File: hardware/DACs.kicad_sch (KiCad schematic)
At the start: 44 parts, among them J10 Conn_Coaxial, J11 Conn_Coaxial, J12 Conn_Coaxial, J9 Conn_Coaxial, U10 LTC2642, U21 LTC2642, U26 REF35250QDBVR, U4 OPA2994xD, U5 OPA2994xD, U6 LTC2642, U7 OPA2994xD, U8 OPA2994xD, U9 LTC2642

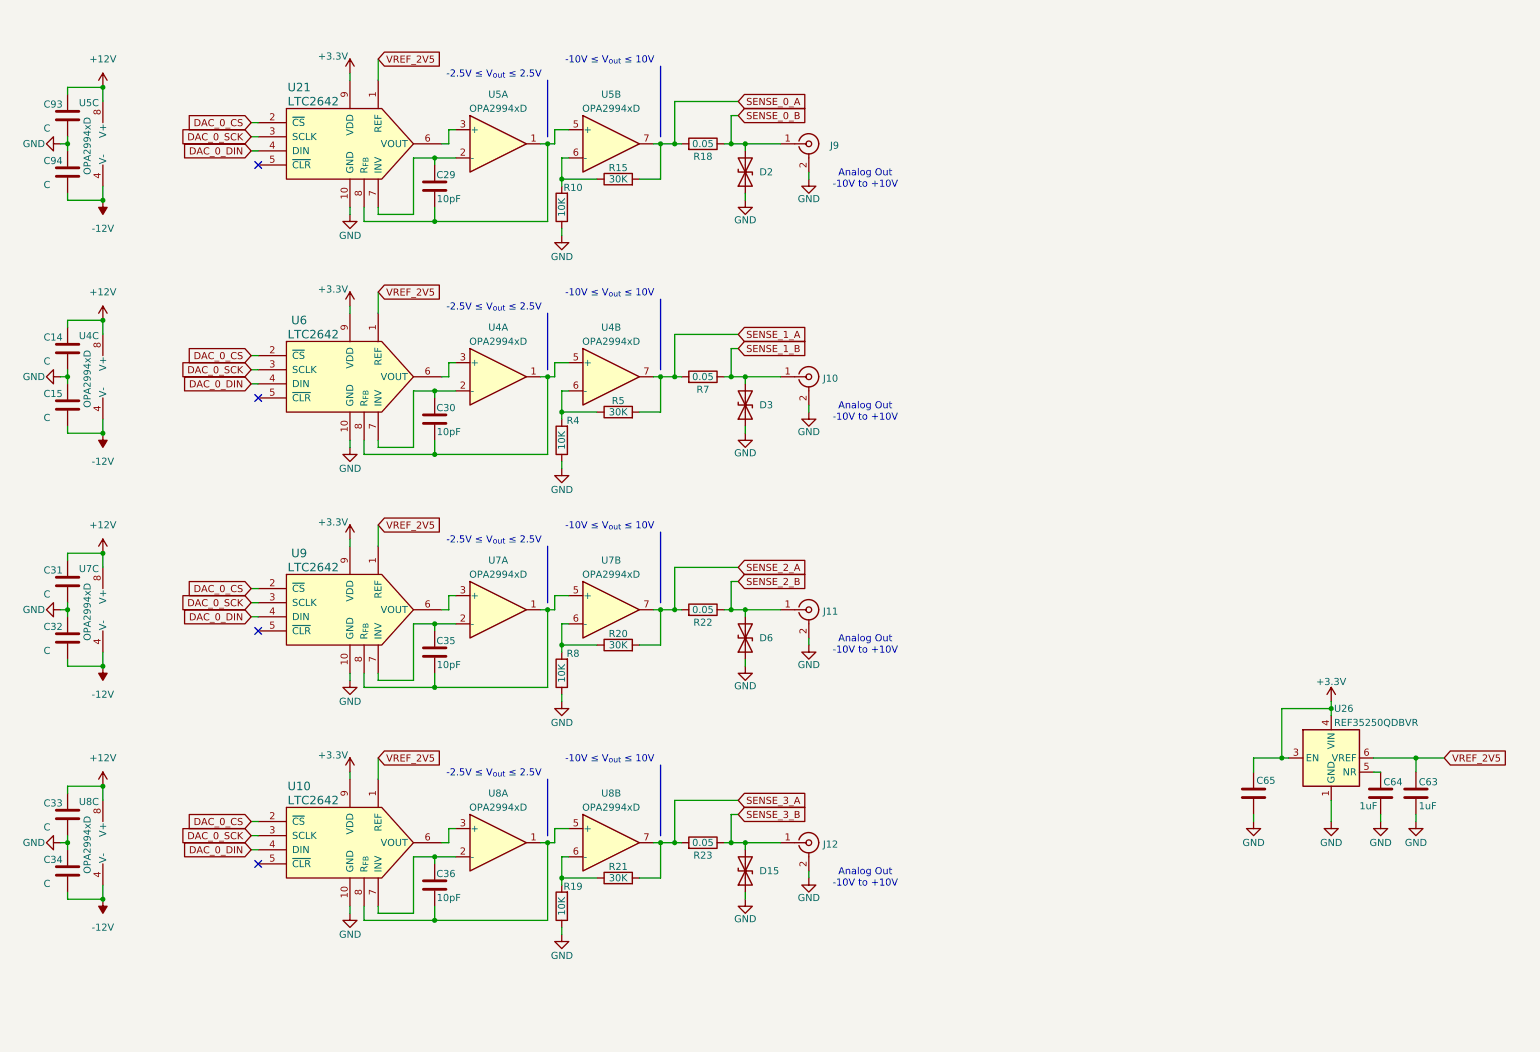
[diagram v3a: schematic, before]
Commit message: update short detection; draft bom
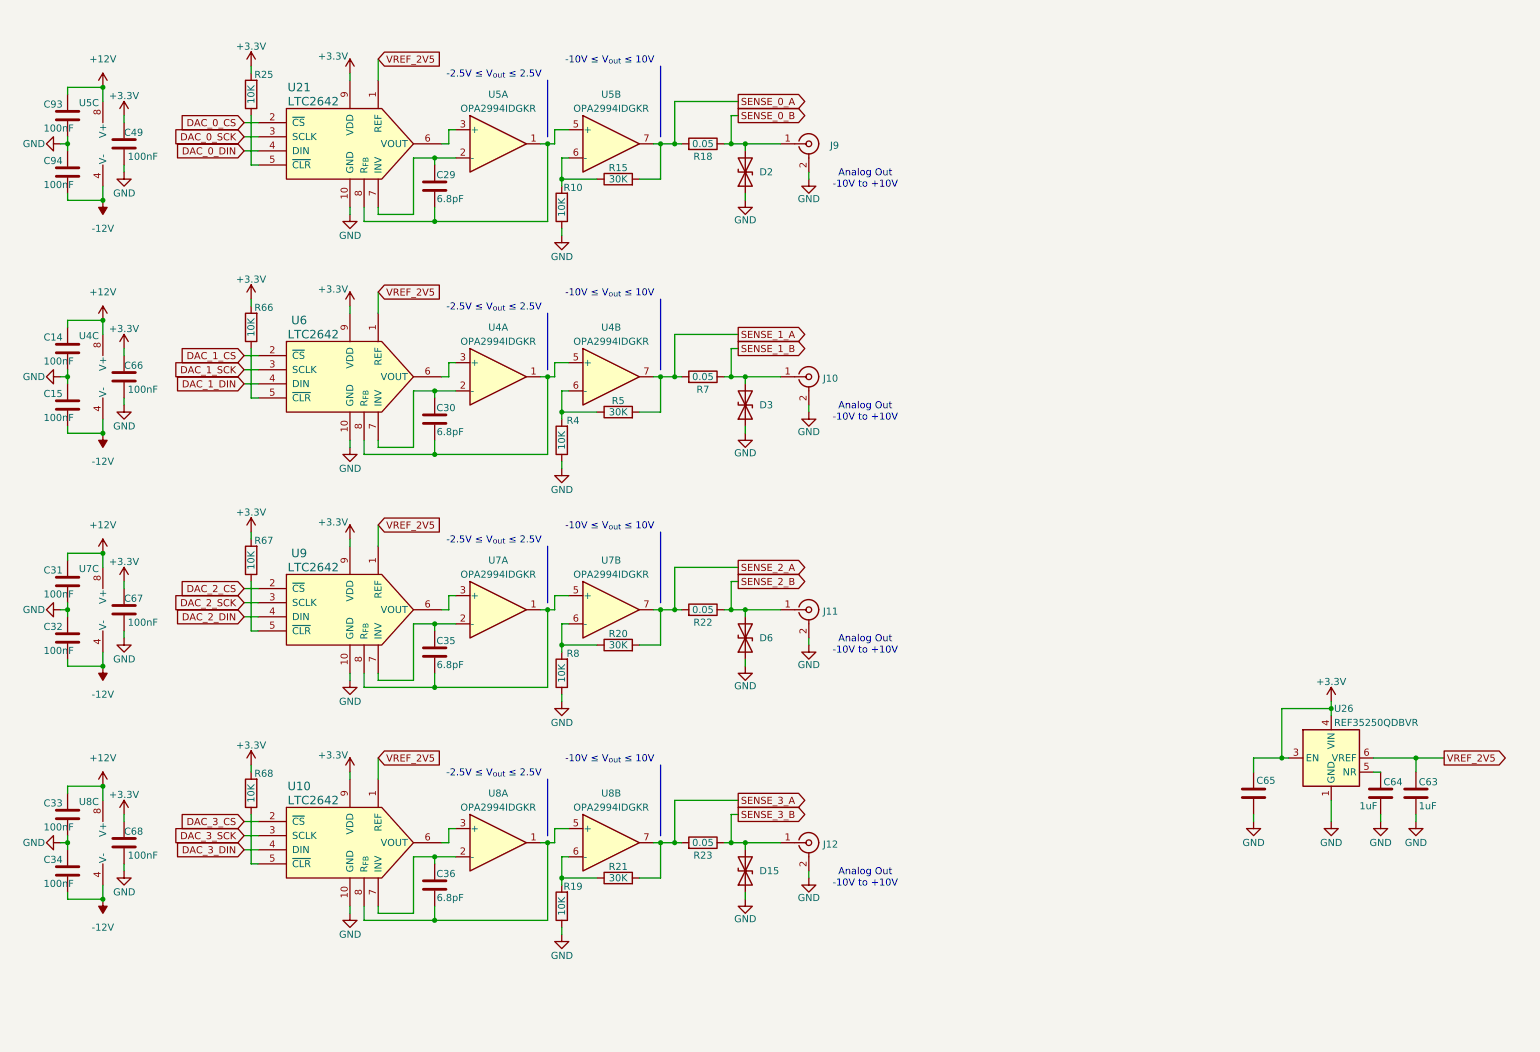
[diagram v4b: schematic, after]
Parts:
- added C49, C66, C67, C68: 100nF, Capacitor_SMD:C_0402_1005Metric, symbol harp.device.quad.dac:C_0603
- added R25, R66, R67, R68: 10K, Resistor_SMD:R_0402_1005Metric, symbol Device:R
- C14, C15, C31, C32, C33, C34, C93, C94: value C -> 100nF; footprint (none) -> Capacitor_SMD:C_0402_1005Metric; Link (none) -> https://www.digikey.com/en/products/detail/murata-electroni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; Manufacturer (none) -> Murata Electronics; Manufacturer Number (none) -> GRM155R71H104KE14D; Temperature Coefficient (none) -> X7R
- C29, C30, C35, C36: value 10pF -> 6.8pF; footprint (none) -> Capacitor_SMD:C_0402_1005Metric; Link (none) -> https://www.digikey.com/en/products/detail/murata-electroni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; Manufacturer (none) -> Murata Electronics; Manufacturer Number (none) -> GCM1555C1H6R8BA16J; Temperature Coefficient (none) -> C0G/NP0
- C63, C64: Manufacturer_Name TDK -> (none); Manufacturer_Part_Number C1608X7R1H105K080AB -> (none)
- C65: footprint Capacitor_SMD:C_0603_1608Metric -> Capacitor_SMD:C_0402_1005Metric; Link https://www.digikey.com/en/products/detail/kemet/C0603C104K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 -> https://www.digikey.com/en/products/detail/murata-electroni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; Manufacturer KEMET -> Murata Electronics; Manufacturer Number C0603C104K5RACTU -> GRM155R71H104KE14D; Manufacturer_Name KEMET -> (none); Manufacturer_Part_Number C0603C104K5RACTU -> (none); PCBWay Link https://www.pcbway.com/components/detail/0402B104K160CT/307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 -> (none); Temperature Coefficient (none) -> X7R
- R10, R15, R19, R20, R21, R4, R5, R8: footprint (none) -> Resistor_SMD:R_0402_1005Metric
- R18, R22, R23, R7: footprint (none) -> Resistor_SMD:R_0402_1005Metric; Link (none) -> https://www.digikey.com/en/products/detail/panasonic-electr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; Manufacturer (none) -> Panasonic Electronic Components; Manufacturer Number (none) -> ERJ-2BWFR050X
- U10, U21, U6, U9: footprint (none) -> Package_SO:MSOP-10_3x3mm_P0.5mm
- U4, U5, U7, U8: value OPA2994xD -> OPA2994IDGKR; footprint Package_SO:SOIC-8_3.9x4.9mm_P1.27mm -> Package_SO:VSSOP-8_3x3mm_P0.65mm; Manufacturer (none) -> Texas Instruments; Manufacturer Number (none) -> OPA2994IDGKR
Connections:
- net +3.3V: now also C49.2, C66.2, C67.2, C68.2, R25.2, R66.2, R67.2, R68.2
- net DAC_0_CS: no longer U10.2 (~{CS}), U6.2 (~{CS}), U9.2 (~{CS})
- net DAC_0_DIN: no longer U10.4 (DIN), U6.4 (DIN), U9.4 (DIN)
- net DAC_0_SCK: no longer U10.3 (SCLK), U6.3 (SCLK), U9.3 (SCLK)
- net GND: now also C49.1, C66.1, C67.1, C68.1
- net at U10.5 (~{CLR}): now also R68.1
- net at U9.5 (~{CLR}): now also R67.1
- net at U6.5 (~{CLR}): now also R66.1
- net at U21.5 (~{CLR}): now also R25.1
- new net DAC_1_CS: U6.2 (~{CS})
- new net DAC_1_DIN: U6.4 (DIN)
- new net DAC_1_SCK: U6.3 (SCLK)
- new net DAC_2_CS: U9.2 (~{CS})
- new net DAC_2_DIN: U9.4 (DIN)
- new net DAC_2_SCK: U9.3 (SCLK)
- new net DAC_3_CS: U10.2 (~{CS})
- new net DAC_3_DIN: U10.4 (DIN)
- new net DAC_3_SCK: U10.3 (SCLK)
- no-connect marks 4 -> 0

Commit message: update board draft
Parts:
- J6: renamed from J9; footprint harp.device.quad.dac.kicad:SMA_TE_Connectivity_CONSMA002-SMD-G-T_Horizontal -> kicad-lib:BNC_TEConnectivity_CONBNC001_Vertical; Link https://www.digikey.com/en/products/detail/te-connectivity-linx/CONSMA002-SMD-G-T/10524518 -> https://www.digikey.com/en/products/detail/te-connectivity-linx/CONBNC001/16013844; Manufacturer Number CONSMA002-SMD-G-T -> CONBNC001
- J7: renamed from J10; footprint harp.device.quad.dac.kicad:SMA_TE_Connectivity_CONSMA002-SMD-G-T_Horizontal -> kicad-lib:BNC_TEConnectivity_CONBNC001_Vertical; Link https://www.digikey.com/en/products/detail/te-connectivity-linx/CONSMA002-SMD-G-T/10524518 -> https://www.digikey.com/en/products/detail/te-connectivity-linx/CONBNC001/16013844; Manufacturer Number CONSMA002-SMD-G-T -> CONBNC001
- J8: renamed from J11; footprint harp.device.quad.dac.kicad:SMA_TE_Connectivity_CONSMA002-SMD-G-T_Horizontal -> kicad-lib:BNC_TEConnectivity_CONBNC001_Vertical; Link https://www.digikey.com/en/products/detail/te-connectivity-linx/CONSMA002-SMD-G-T/10524518 -> https://www.digikey.com/en/products/detail/te-connectivity-linx/CONBNC001/16013844; Manufacturer Number CONSMA002-SMD-G-T -> CONBNC001
- J9: renamed from J12; footprint harp.device.quad.dac.kicad:SMA_TE_Connectivity_CONSMA002-SMD-G-T_Horizontal -> kicad-lib:BNC_TEConnectivity_CONBNC001_Vertical; Link https://www.digikey.com/en/products/detail/te-connectivity-linx/CONSMA002-SMD-G-T/10524518 -> https://www.digikey.com/en/products/detail/te-connectivity-linx/CONBNC001/16013844; Manufacturer Number CONSMA002-SMD-G-T -> CONBNC001
- renumbered C93 to C31, C94 to C32, C14 to C33, C15 to C34, C31 to C35, C32 to C36, C33 to C37, C34 to C38, C49 to C39, C66 to C40, C67 to C41, C68 to C42, C29 to C43, C30 to C44, C35 to C45, C36 to C46, C65 to C47, C64 to C48, C63 to C49, D15 to D10, D2 to D7, D3 to D8, D6 to D9, R25 to R23, R66 to R24, R67 to R25, R68 to R26, R10 to R27, R4 to R28, R8 to R29, R19 to R30, R15 to R31, R5 to R32, R20 to R33, R21 to R34, R18 to R35, R7 to R36, R22 to R37, R23 to R38, U9 to U10, U10 to U11, U26 to U12, U5 to U4, U4 to U5, U7 to U6, U8 to U7, U21 to U8, U6 to U9

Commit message: update pcb
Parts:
- added R1, R19, R22, R4: 10K, Resistor_SMD:R_0402_1005Metric, symbol Device:R
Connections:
- net +3.3V: now also R1.2, R19.2, R22.2, R4.2
- net DAC_0_CS: now also R22.1
- net DAC_1_CS: now also R19.1
- net DAC_2_CS: now also R4.1
- net DAC_3_CS: now also R1.1
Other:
- moved on the sheet: C43, C44, C45, C46, D10, D7, D8, D9, J6, J7, J8, J9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

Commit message: update bom
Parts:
- R1, R19, R22, R23, R24, R25, R26, R27, R28, R29, R30, R4: Link (none) -> https://www.digikey.com/en/products/detail/samsung-electro-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; Manufacturer (none) -> Samsung Electro-Mechanics; Manufacturer Number (none) -> RC1005F103CS
- R31, R32, R33, R34: Link (none) -> https://www.digikey.com/en/products/detail/panasonic-electr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; Manufacturer (none) -> Panasonic Electronic Components; Manufacturer Number (none) -> ERA-2AEB303X
- U12: value REF35250QDBVR -> REF3525; Link (none) -> https://mou.sr/45eDj2t; Manufacturer (none) -> Texas Instruments; Manufacturer Number (none) -> REF35250QDBVRQ1
